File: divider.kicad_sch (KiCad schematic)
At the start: 2 parts

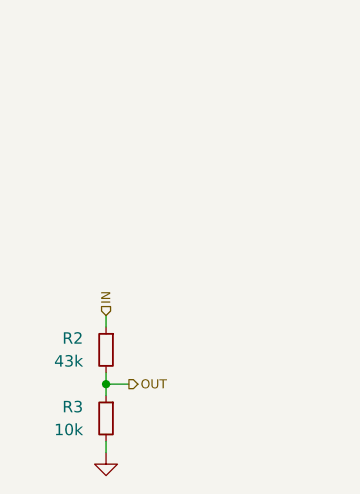
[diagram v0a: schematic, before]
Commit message: schematic: Tentatively finish major schematic parts
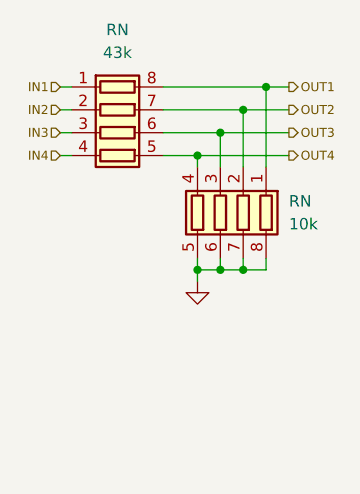
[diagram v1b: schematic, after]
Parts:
- removed R2: 43k, symbol Device:R_Small
- removed R3: 10k, symbol Device:R_Small
- added RN: 10k, symbol Device:R_Pack04
- added RN: 43k, symbol Device:R_Pack04
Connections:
- net GND: now also RN.5 (R4.2), RN.6 (R3.2), RN.7 (R2.2), RN.8 (R1.2)
- new net IN1: RN.1 (R1.1)
- new net IN2: RN.2 (R2.1)
- new net IN3: RN.3 (R3.1)
- new net IN4: RN.4 (R4.1)
- new net OUT1: RN.1 (R1.1), RN.8 (R1.2)
- new net OUT2: RN.2 (R2.1), RN.7 (R2.2)
- new net OUT3: RN.3 (R3.1), RN.6 (R3.2)
- new net OUT4: RN.4 (R4.1), RN.5 (R4.2)
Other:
- company: (none) -> York Formula Student
- title: (none) -> Rear Distribution

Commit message: schematic: Re-annotate and add RTC battery
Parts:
- renumbered RN to RN1, RN to RN2
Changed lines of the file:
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@@
 		(dnp no)
 		(fields_autoplaced yes)
-		(property "Reference" "RN"
+		(property "Reference" "RN2"
 			(at 114.3 41.9099 0)
 			(effects
@@
 				(path "/f2809c69-a8f9-4542-bde7-ba954770c514/010a91b4-d570-4701-8f82-257b9f40c4fc"
 					(reference "RN4")
+					(unit 1)
+				)
+				(path "/f2809c69-a8f9-4542-bde7-ba954770c514/63292095-4e17-4494-84a6-c656f1d2ccc4"
+					(reference "RN2")
 					(unit 1)
 				)
@@
 		(on_board yes)
 		(dnp no)
-		(property "Reference" "RN"
+		(property "Reference" "RN1"
 			(at 95.25 22.86 90)
 			(effects
@@
 				(path "/f2809c69-a8f9-4542-bde7-ba954770c514/010a91b4-d570-4701-8f82-257b9f40c4fc"
 					(reference "RN3")
+					(unit 1)
+				)
+				(path "/f2809c69-a8f9-4542-bde7-ba954770c514/63292095-4e17-4494-84a6-c656f1d2ccc4"
+					(reference "RN1")
 					(unit 1)
 				)
@@
 		(dnp no)
 		(fields_autoplaced yes)
-		(property "Reference" "#PWR051"
+		(property "Reference" "#PWR0181"
 			(at 104.14 57.15 0)
 			(effects
@@
 			(project "rear_distribution"
 				(path "/f2809c69-a8f9-4542-bde7-ba954770c514/010a91b4-d570-4701-8f82-257b9f40c4fc"
-					(reference "#PWR050")
+					(reference "#PWR0182")
 					(unit 1)
 				)
 				(path "/f2809c69-a8f9-4542-bde7-ba954770c514/63292095-4e17-4494-84a6-c656f1d2ccc4"
-					(reference "#PWR051")
+					(reference "#PWR0181")
 					(unit 1)
 				)
 				(path "/f2809c69-a8f9-4542-bde7-ba954770c514/7b4c8936-a39b-45f9-86af-2e1af62e4938"
-					(reference "#PWR055")
+					(reference "#PWR0186")
 					(unit 1)
 				)
 				(path "/f2809c69-a8f9-4542-bde7-ba954770c514/95a6bef4-8501-44cc-b21b-7ddf3b97e37a"
-					(reference "#PWR053")
+					(reference "#PWR0184")
 					(unit 1)
 				)
 				(path "/f2809c69-a8f9-4542-bde7-ba954770c514/c71d5a16-8ff3-47fd-8809-f0c518346052"
-					(reference "#PWR054")
+					(reference "#PWR0185")
 					(unit 1)
 				)
 				(path "/f2809c69-a8f9-4542-bde7-ba954770c514/f9195b01-e564-4cb3-9d3d-bb998dddd574"
-					(reference "#PWR052")
-					(unit 1)
-				)
+					(reference "#PWR0183")
+					(unit 1)
+				)

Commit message: schematic: Assign footprints and fill most of BOM
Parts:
- RN1, RN2: footprint (none) -> Resistor_SMD:R_Array_Convex_4x1206
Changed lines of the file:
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@@
 			)
 		)
-		(property "Footprint" ""
+		(property "Footprint" "Resistor_SMD:R_Array_Convex_4x1206"
 			(at 99.695 43.18 90)
 			(effects
@@
 			)
 		)
-		(property "Footprint" ""
+		(property "Footprint" "Resistor_SMD:R_Array_Convex_4x1206"
 			(at 95.25 41.275 90)
 			(effects

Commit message: schematic: Cleanup BOM
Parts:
- RN1: DigiKey # (none) -> 13-YC324-JK-0747KLCT-ND; LCSC # (none) -> C877007; Mfr (none) -> YAGEO; Mfr # (none) -> YC324-JK-0747KL; Mouser # (none) -> 603-YC324-FK-0747KL
- RN2: DigiKey # (none) -> 13-YC324-FK-0710KLCT-ND; LCSC # (none) -> C876914; Mfr (none) -> YAGEO; Mfr # (none) -> YC324-FK-0710KL; Mouser # (none) -> 603-YC324-FK-0710KL
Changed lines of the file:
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@@
+			)
+		)
+		(property "DigiKey #" "13-YC324-FK-0710KLCT-ND"
+			(at 106.68 43.18 0)
+			(effects
+				(font
+					(size 1.27 1.27)
+				)
+				(hide yes)
+			)
+		)
+		(property "LCSC #" "C876914"
+			(at 106.68 43.18 0)
+			(effects
+				(font
+					(size 1.27 1.27)
+				)
+				(hide yes)
+			)
+		)
+		(property "Mfr" "YAGEO"
+			(at 106.68 43.18 0)
+			(effects
+				(font
+					(size 1.27 1.27)
+				)
+				(hide yes)
+			)
+		)
+		(property "Mfr #" "YC324-FK-0710KL"
+			(at 106.68 43.18 0)
+			(effects
+				(font
+					(size 1.27 1.27)
+				)
+				(hide yes)
+			)
+		)
+		(property "Mouser #" "603-YC324-FK-0710KL"
+			(at 106.68 43.18 0)
+			(effects
+				(font
+					(size 1.27 1.27)
+				)
+				(hide yes)
 			)
 		)
@@
 			(effects
 				(font
+					(size 1.27 1.27)
+				)
+				(hide yes)
+			)
+		)
+		(property "DigiKey #" "13-YC324-JK-0747KLCT-ND"
+			(at 95.25 34.29 90)
+			(effects
+				(font
+					(size 1.27 1.27)
+				)
+				(hide yes)
+			)
+		)
+		(property "LCSC #" "C877007"
+			(at 95.25 34.29 90)
+			(effects
+				(font
+					(size 1.27 1.27)
+				)
+				(hide yes)
+			)
+		)
+		(property "Mfr" "YAGEO"
+			(at 95.25 34.29 90)
+			(effects
+				(font
+					(size 1.27 1.27)
+				)
+				(hide yes)
+			)
+		)
+		(property "Mfr #" "YC324-JK-0747KL"
+			(at 95.25 34.29 90)
+			(effects
+				(font
+					(size 1.27 1.27)
+				)
+				(hide yes)
+			)
+		)
+		(property "Mouser #" "603-YC324-FK-0747KL"
+			(at 95.25 34.29 90)
+			(effects
+				(font
